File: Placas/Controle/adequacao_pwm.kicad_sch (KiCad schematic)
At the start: 9 parts, among them Q4 BC337, U21 H11L1

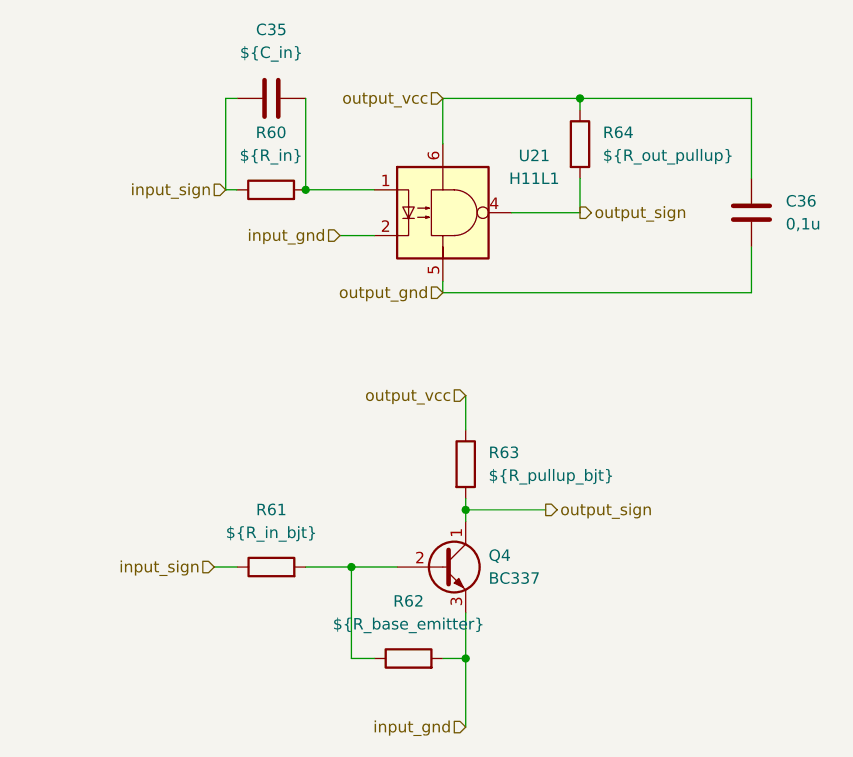
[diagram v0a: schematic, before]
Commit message: Modificações nas duas placas, adição de furos para montagem, melhora na posição dos micros e conectores para comunicação SPI
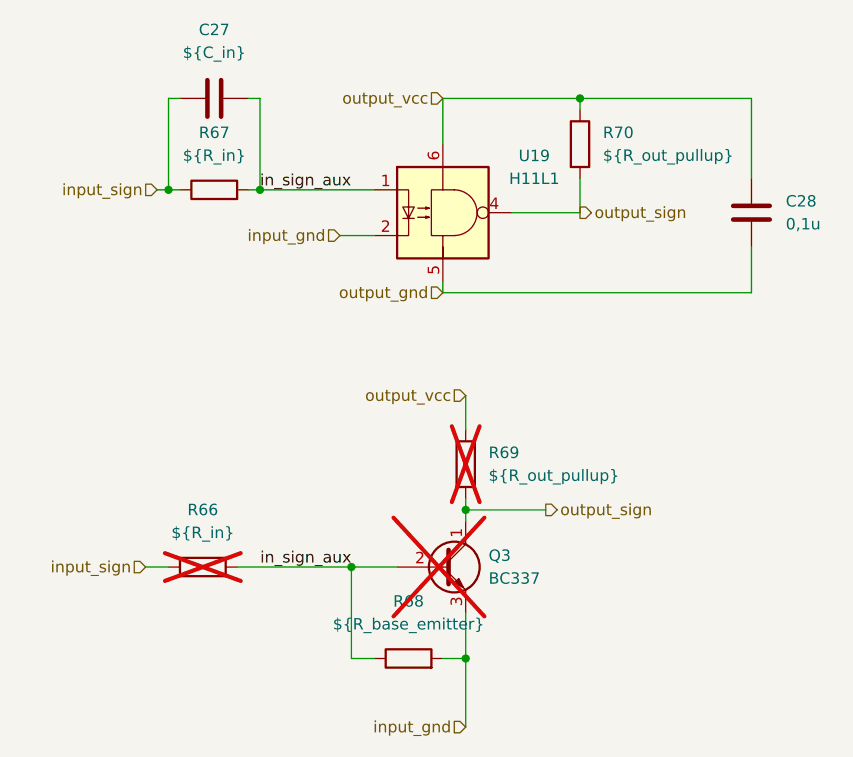
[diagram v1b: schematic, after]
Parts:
- C27: renamed from C35; footprint Capacitor_THT:C_Disc_D8.0mm_W5.0mm_P7.50mm -> Capacitor_SMD:C_0805_2012Metric_Pad1.18x1.45mm_HandSolder
- C28: renamed from C36; footprint Capacitor_THT:C_Disc_D8.0mm_W5.0mm_P7.50mm -> Capacitor_SMD:C_0805_2012Metric_Pad1.18x1.45mm_HandSolder
- Q3: renamed from Q4; now not fitted
- R66: renamed from R61; value ${R_in_bjt} -> ${R_in}; now not fitted
- R67: renamed from R60; footprint Resistor_THT:R_Axial_DIN0207_L6.3mm_D2.5mm_P7.62mm_Horizontal -> Resistor_SMD:R_0805_2012Metric_Pad1.20x1.40mm_HandSolder
- R68: renamed from R62; footprint Resistor_THT:R_Axial_DIN0207_L6.3mm_D2.5mm_P7.62mm_Horizontal -> Resistor_SMD:R_0805_2012Metric_Pad1.20x1.40mm_HandSolder
- R69: renamed from R63; value ${R_pullup_bjt} -> ${R_out_pullup}; now not fitted
- R70: renamed from R64; footprint Resistor_THT:R_Axial_DIN0207_L6.3mm_D2.5mm_P7.62mm_Horizontal -> Resistor_SMD:R_0805_2012Metric_Pad1.20x1.40mm_HandSolder
- renumbered U21 to U19
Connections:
- net in_sign_aux: now reaches Q3.2 (B), R66.2, R68.1
- net in_sign_aux: now also C27.2, R67.2, U19.1
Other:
- moved on the sheet: C27, R67

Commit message: Criação de novas pastas com código em C e Matlab
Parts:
- R68: now not fitted
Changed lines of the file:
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@@
 		(in_bom yes)
 		(on_board yes)
-		(dnp no)
+		(dnp yes)
 		(fields_autoplaced yes)
 		(property "Reference" "R68"

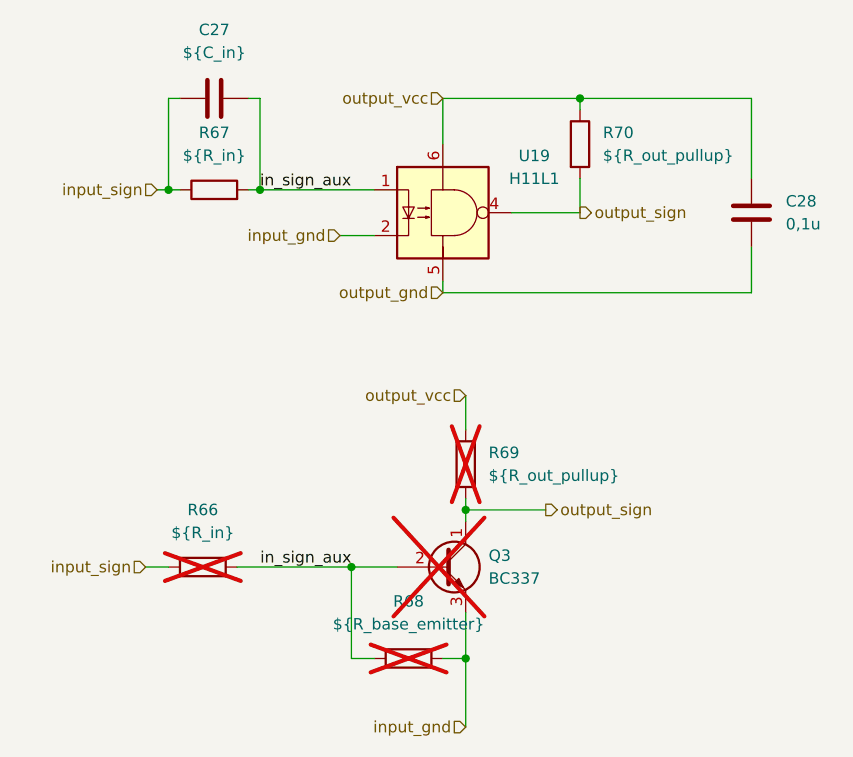
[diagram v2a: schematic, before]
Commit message: Mudanças no firmware e calibração da tensão de entrada e saída
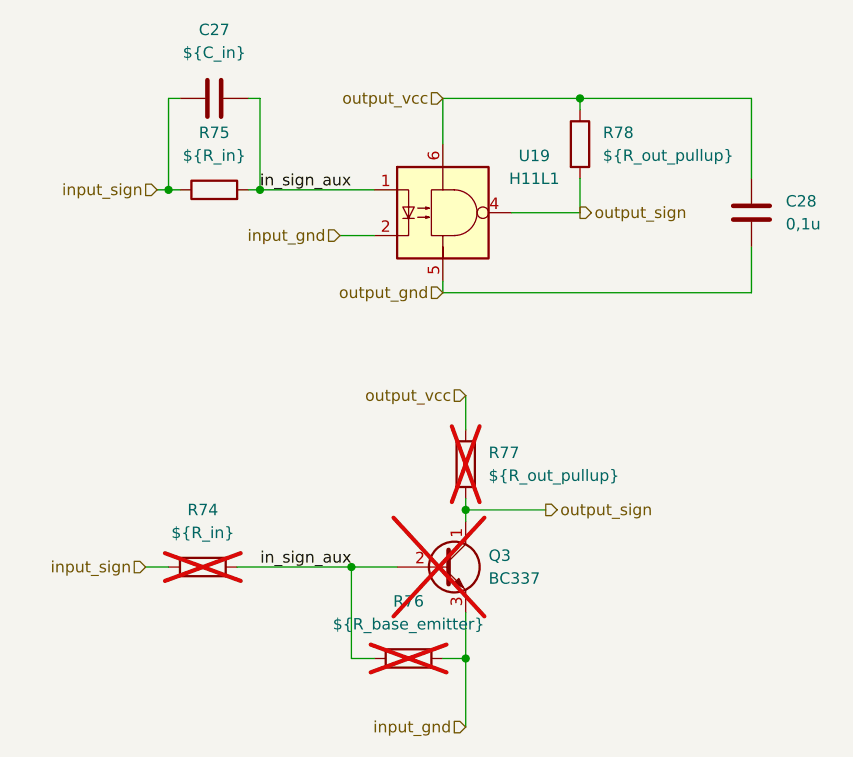
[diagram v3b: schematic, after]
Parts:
- renumbered R66 to R74, R67 to R75, R68 to R76, R69 to R77, R70 to R78
